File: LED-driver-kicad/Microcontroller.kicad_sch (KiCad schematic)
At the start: 2 parts, among them U6 PIC16F18026-ISL, U9 25AA02E64T-I/OT

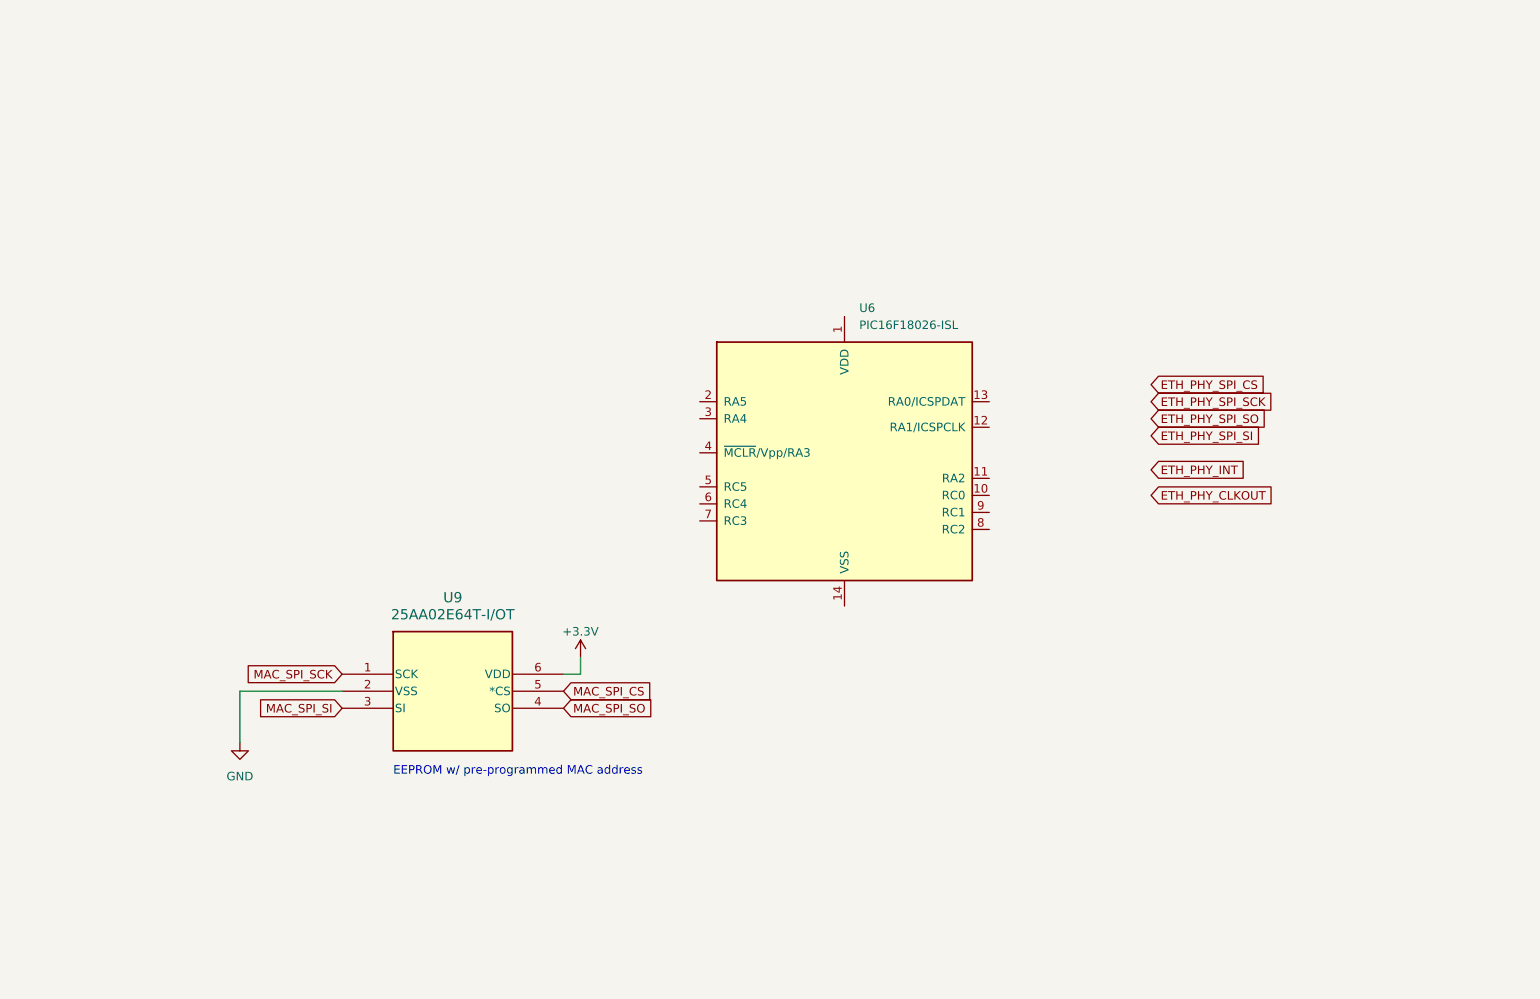
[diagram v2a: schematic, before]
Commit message: update schematic for main microcontroller
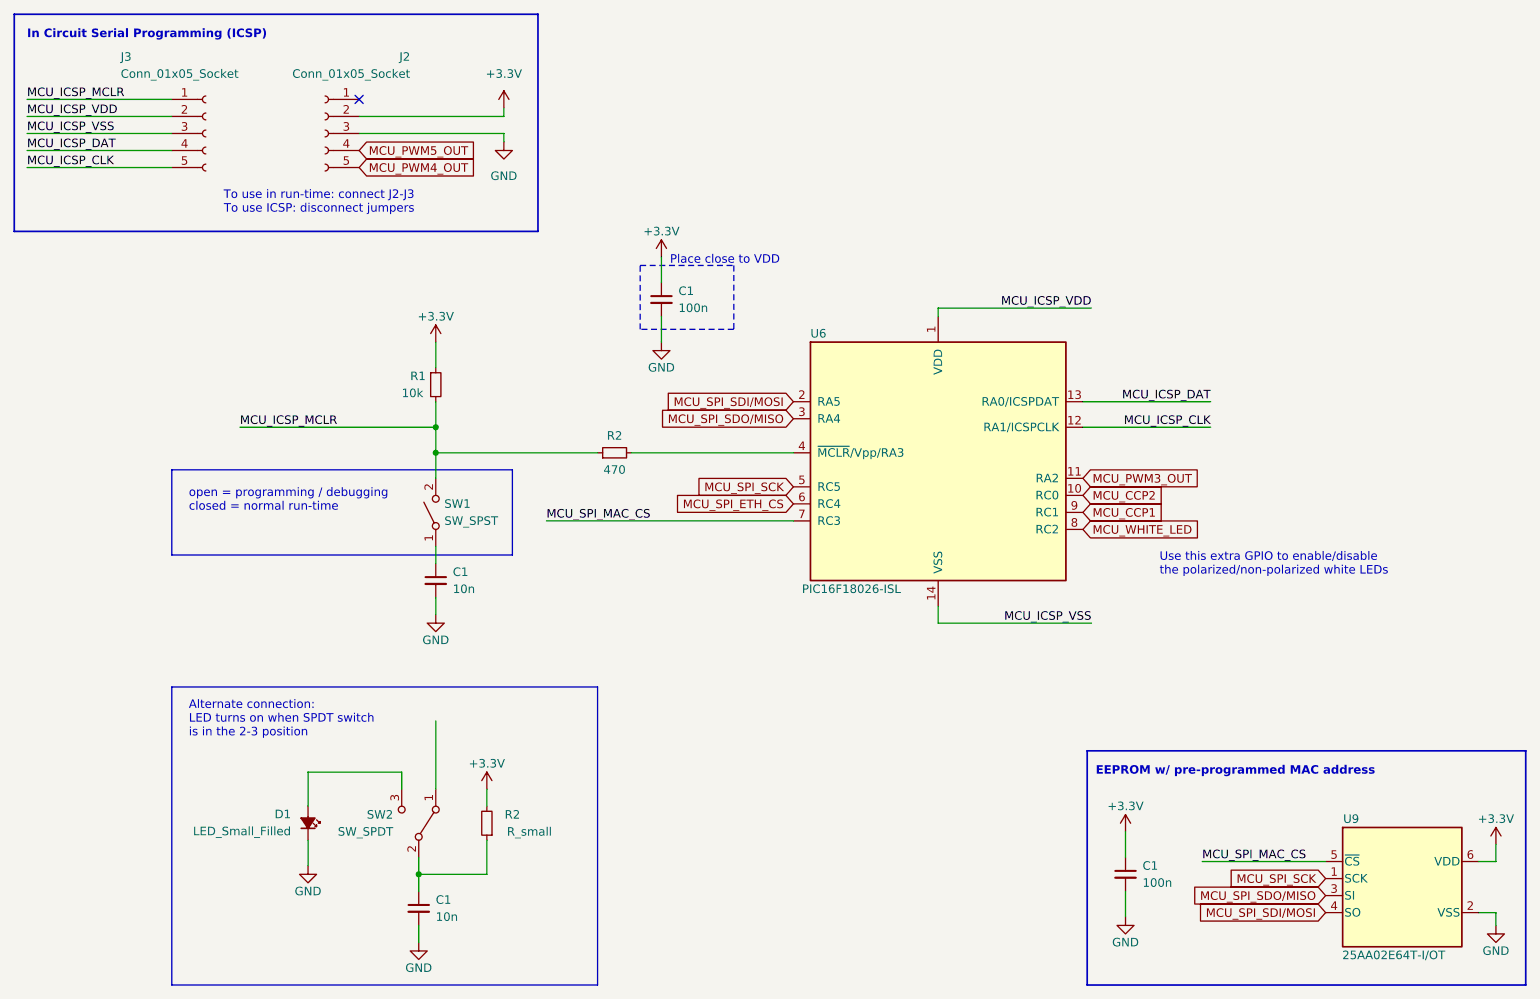
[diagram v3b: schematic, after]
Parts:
- added C1 (x2): 100n, symbol Device:C_Small
- added C1 (x2): 10n, symbol Device:C_Small
- added D1: LED_Small_Filled, symbol Device:LED_Small_Filled
- added J2, J3: Conn_01x05_Socket, symbol Connector:Conn_01x05_Socket
- added R1: 10k, symbol Device:R_Small
- added R2: 470, symbol Device:R_Small
- added R2: R_small, symbol Device:R_Small
- added SW1: SW_SPST, symbol Switch:SW_SPST
- added SW2: SW_SPDT, symbol Switch:SW_SPDT
- U9: footprint SOT-23-6_MC_MCH -> Mahabeer_Package_SOT_SMD:SOT-23-6_MC_MCH-Memory_Microchip_25AA02E64T-IOT
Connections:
- net MAC_SPI_CS is gone; now on net MCU_SPI_MAC_CS: U9.5 (~{CS})
- net MAC_SPI_SCK is gone; now on net MCU_SPI_SCK: U9.1 (SCK)
- net MAC_SPI_SI is gone; now on net MCU_SPI_SDO/MISO: U9.3 (SI)
- net MAC_SPI_SO is gone; now on net MCU_SPI_SDI/MOSI: U9.4 (SO)
- net +3.3V: now also C1.1, C1.1, J2.2 (Pin_2), R1.1, R2.2
- net GND: now also C1.2, C1.2, C1.2, C1.2, D1.1 (K), J2.3 (Pin_3)
- net MCU_ICSP_VDD: now reaches U6.1 (VDD)
- net MCU_ICSP_VDD: now also J3.2 (Pin_2)
- net MCU_CCP2: now reaches U6.10 (RC0)
- net MCU_PWM3_OUT: now reaches U6.11 (RA2)
- net MCU_ICSP_CLK: now reaches U6.12 (RA1/ICSPCLK)
- net MCU_ICSP_CLK: now also J3.5 (Pin_5)
- net MCU_ICSP_DAT: now reaches U6.13 (RA0/ICSPDAT)
- net MCU_ICSP_DAT: now also J3.4 (Pin_4)
- net MCU_ICSP_VSS: now reaches U6.14 (VSS)
- net MCU_ICSP_VSS: now also J3.3 (Pin_3)
- net MCU_SPI_SDI/MOSI: now reaches U6.2 (RA5)
- net MCU_SPI_SDO/MISO: now reaches U6.3 (RA4)
- net at U6.4 (~{MCLR}/Vpp/RA3): now also R2.2
- net MCU_SPI_SCK: now reaches U6.5 (RC5)
- net MCU_SPI_ETH_CS: now reaches U6.6 (RC4)
- net MCU_SPI_MAC_CS: now reaches U6.7 (RC3)
- net MCU_WHITE_LED: now reaches U6.8 (RC2)
- net MCU_CCP1: now reaches U6.9 (RC1)
- new net: C1.1, SW1.1 (A)
- new net: C1.1, R2.1, SW2.2 (B)
- new net: D1.2 (A), SW2.3 (C)
- new net MCU_ICSP_MCLR: J3.1 (Pin_1), R1.2, R2.1, SW1.2 (B)
- new net MCU_PWM4_OUT: J2.5 (Pin_5)
- new net MCU_PWM5_OUT: J2.4 (Pin_4)
- no-connect marks 0 -> 1
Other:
- note added: "Alternate connection: LED turns on when SPDT switch is in the 2-3 position"
- note added: "In Circuit Serial Programming (ICSP)"
- note added: "Place close to VDD"
- note added: "To use in run-time: connect J2-J3 To use ICSP: disconnect jumpers"
- note added: "Use this extra GPIO to enable/disable the polarized/non-polarized white LEDs"
- note added: "open = programming / debugging closed = normal run-time"
- moved on the sheet: U6, U9

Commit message: update *MCLR switch for microcontroller
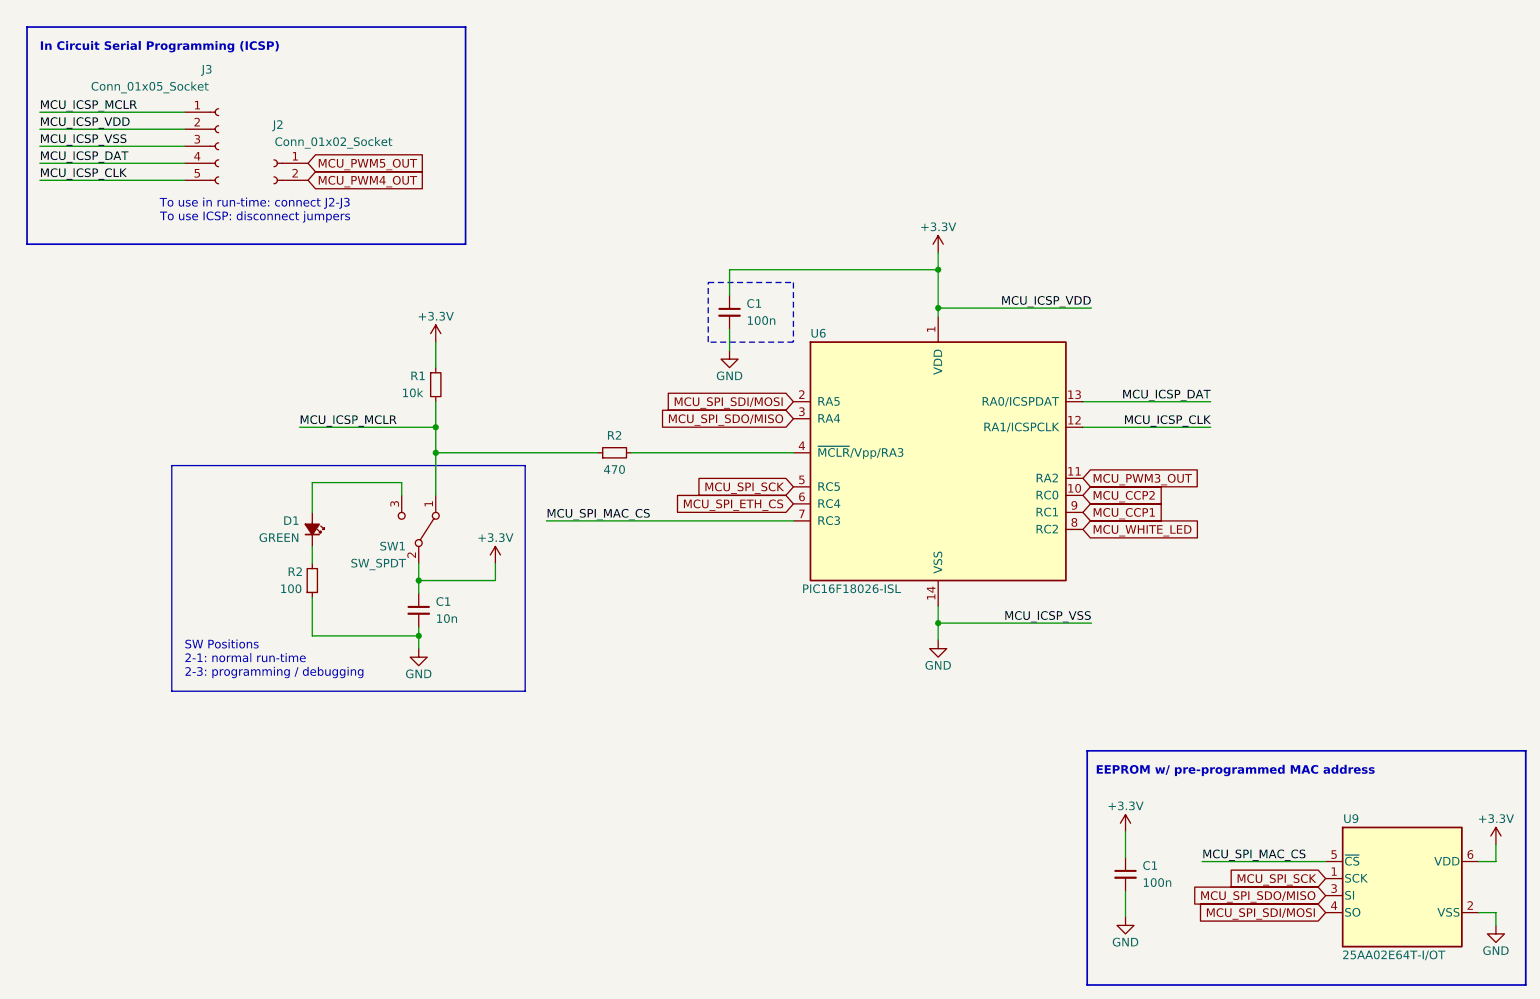
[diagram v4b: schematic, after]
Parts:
- removed C1: 10n, symbol Device:C_Small
- removed J2: Conn_01x05_Socket, symbol Connector:Conn_01x05_Socket
- removed SW1: SW_SPST, symbol Switch:SW_SPST
- added J2: Conn_01x02_Socket, symbol Connector:Conn_01x02_Socket
- D1: value LED_Small_Filled -> GREEN
- R2: value R_small -> 100
- renumbered SW2 to SW1
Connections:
- net MCU_ICSP_VDD is gone; now on net +3.3V: J3.2 (Pin_2), U6.1 (VDD)
- net MCU_ICSP_VSS is gone; now on net GND: J3.3 (Pin_3), U6.14 (VSS)
- net +3.3V: now also C1.1, SW1.2 (B); no longer R2.2
- net GND: now also R2.1; no longer D1.1 (K)
- net MCU_ICSP_MCLR: now also SW1.1 (A)
- net MCU_PWM4_OUT: now also J2.2 (Pin_2)
- net MCU_PWM5_OUT: now also J2.1 (Pin_1)
- new net: D1.1 (K), R2.2
- no-connect marks 1 -> 0
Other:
- note added: "SW Positions 2-1: normal run-time 2-3: programming / debugging"
- note removed: "Alternate connection: LED turns on when SPDT switch is in the 2-3 position"
- note removed: "Place close to VDD"
- note removed: "Use this extra GPIO to enable/disable the polarized/non-polarized white LEDs"
- note removed: "open = programming / debugging closed = normal run-time"
- moved on the sheet: C1, D1, J3, SW1
